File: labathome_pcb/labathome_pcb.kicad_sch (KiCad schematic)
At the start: 48 parts, among them J11 USB_ESP32, J15 CAN RS 485, J17 Micro_SD_Card_Det1, J21 GPIO, J22 Volts, J6 I2C, J7 PROG ESP, Q6 IRLML6344, SW2 YELLOW, SW3 GREEN, SW3 Reset, SW4 RED, U2 ESP32-S3-WROOM-1, U3 SRV05-4, X2 Display_1.3inch

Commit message: Optimized PCB
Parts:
- removed JP6, JP7: STEP3_EN, Jumper:SolderJumper-2_P1.3mm_Bridged2Bar_RoundedPad1.0x1.5mm, symbol Jumper:Jumper_2_Bridged
- added J18: TC-2030, Connector:Tag-Connect_TC2030-IDC-NL_2x03_P1.27mm_Vertical, symbol Connector:Conn_ARM_SWD_TagConnect_TC2030-NL
- J7: footprint liebler_CONN:PinHeader_2x03_P1.27mm_Vertical_SMD_handsolder -> Connector:Tag-Connect_TC2030-IDC-NL_2x03_P1.27mm_Vertical
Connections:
- net +3V3: now also J18.1 (VCC)
- net GND: now also J18.5 (GND)
- net at U2.28 (SPIIO6/GPIO35/FSPID/SUBSPID): now also JP3.1 (A)
- net at U2.30 (SPIDQS/GPIO37/FSPIQ/SUBSPIQ): no longer JP3.1 (A)
- new net STM32_RESET: J18.3 (~{RESET})
- new net SWCLK: J18.4 (SWCLK)
- new net SWDIO: J18.2 (SWDIO)
- new net UART4_TX: J18.6 (SWO)
- no-connect marks 5 -> 7

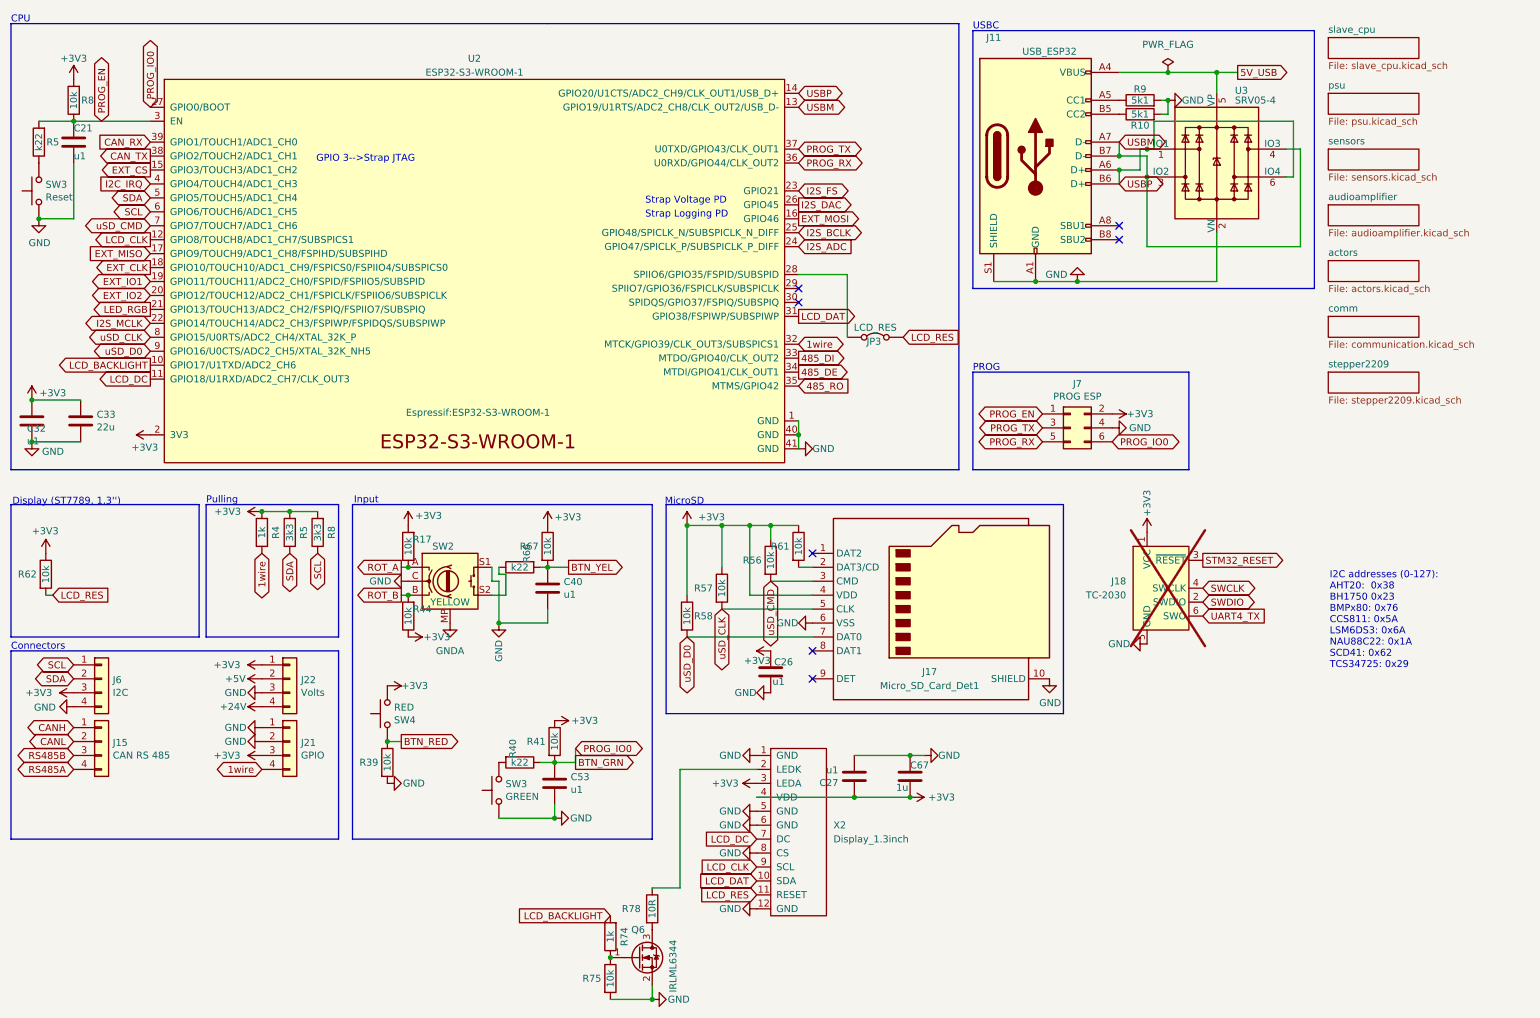
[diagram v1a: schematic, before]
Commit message: Continued with severe refactoring. Now builds, but completely untested
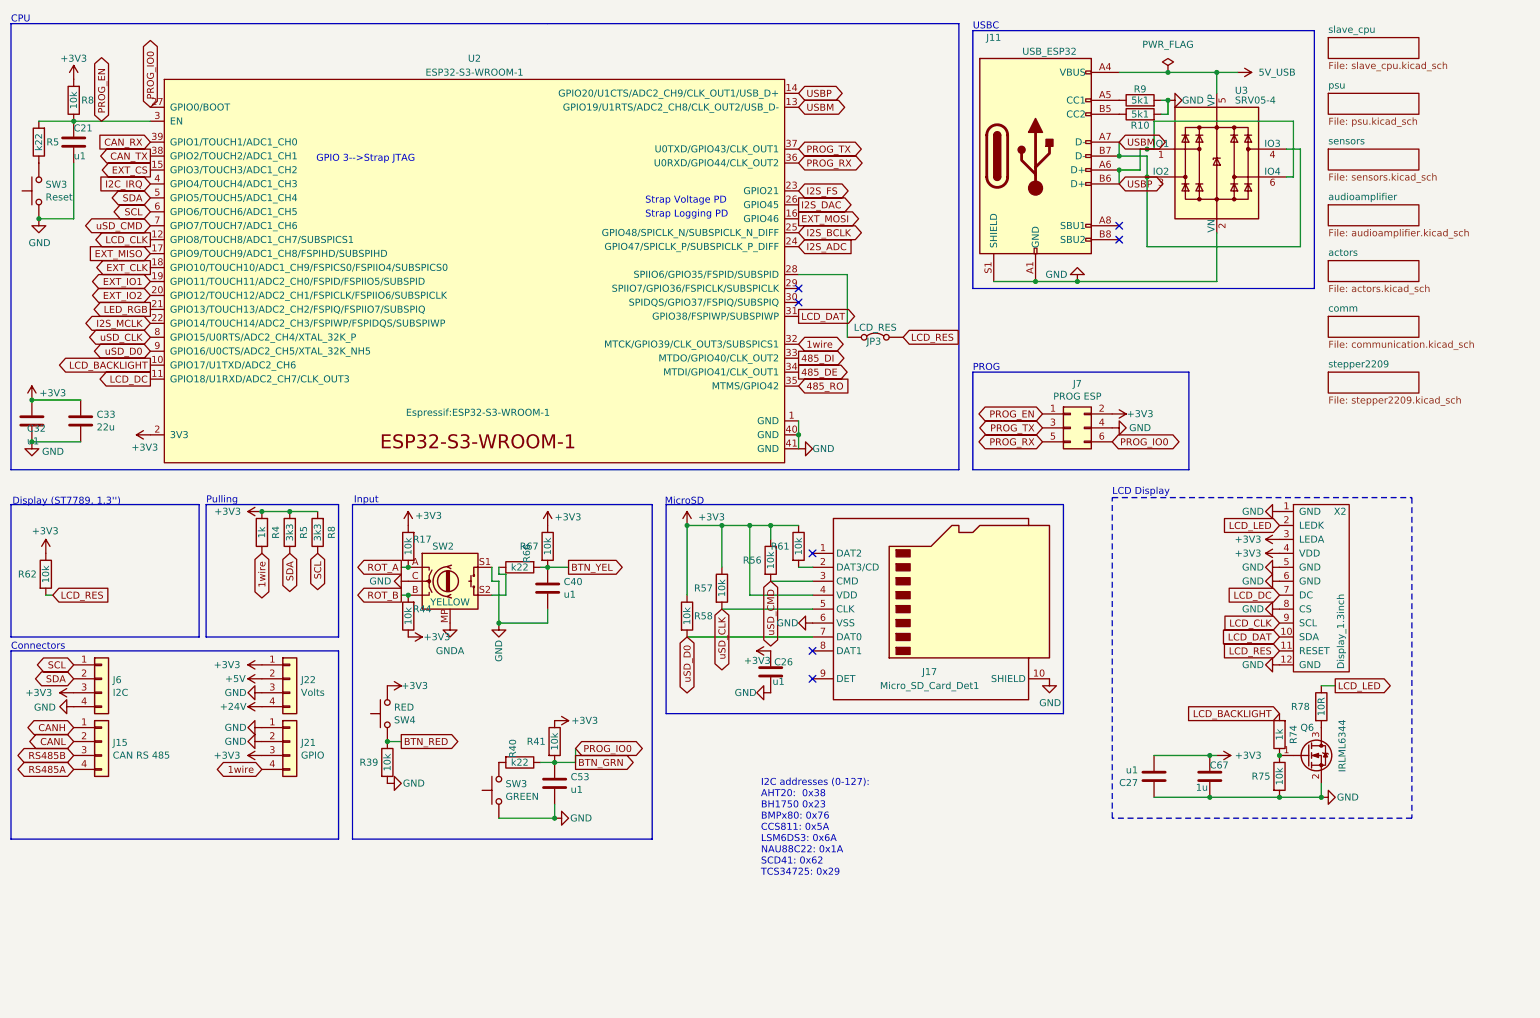
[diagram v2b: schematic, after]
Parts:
- removed J18: TC-2030, Connector:Tag-Connect_TC2030-IDC-NL_2x03_P1.27mm_Vertical, symbol Connector:Conn_ARM_SWD_TagConnect_TC2030-NL
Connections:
- net +3V3: now also C27.2, C67.1; no longer C27.1, C67.2
- net GND: now also C27.1, C67.2; no longer C27.2, C67.1
- net LCD_LED: now reaches R78.1, X2.2 (LEDK)
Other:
- note added: "LCD Display"
- moved on the sheet: C27, C67, Q6, R74, R75, R78, X2

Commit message: Bus servos
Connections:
- net +24V renamed 5-24V
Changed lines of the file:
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@@
-	)
-	(symbol
-		(lib_id "power:+24V")
-		(at 58.42 138.43 90)
-		(unit 1)
-		(exclude_from_sim no)
-		(in_bom yes)
-		(on_board yes)
-		(dnp no)
-		(property "Reference" "#PWR0111"
-			(at 62.23 138.43 0)
-			(effects
-				(font
-					(size 1.27 1.27)
-				)
-				(hide yes)
-			)
-		)
-		(property "Value" "+24V"
-			(at 55.626 138.43 90)
-			(effects
-				(font
-					(size 1.27 1.27)
-				)
-				(justify left)
-			)
-		)
-		(property "Footprint" ""
-			(at 58.42 138.43 0)
-			(effects
-				(font
-					(size 1.27 1.27)
-				)
-				(hide yes)
-			)
-		)
-		(property "Datasheet" ""
-			(at 58.42 138.43 0)
-			(effects
-				(font
-					(size 1.27 1.27)
-				)
-				(hide yes)
-			)
-		)
-		(property "Description" "Power symbol creates a global label with name \"+24V\""
-			(at 58.42 138.43 0)
-			(effects
-				(font
-					(size 1.27 1.27)
-				)
-				(hide yes)
-			)
-		)
-		(pin "1"
-		)
-		(instances
-			(project "labathome_pcb15"
-				(path "/e4d6926a-1a8b-424d-97c4-66b6ad87e4ac"
-					(reference "#PWR0111")
-					(unit 1)
-				)
-			)
-		)
 	)
 	(symbol
@@
 					(unit 1)
 				)
+			)
+		)
+	)
+	(symbol
+		(lib_id "power:+VSW")
+		(at 58.42 138.43 90)
+		(unit 1)
+		(exclude_from_sim no)
+		(in_bom yes)
+		(on_board yes)
+		(dnp no)
+		(fields_autoplaced yes)
+		(property "Reference" "#PWR076"
+			(at 62.23 138.43 0)
+			(effects
+				(font
+					(size 1.27 1.27)
+				)
+				(hide yes)
+			)
+		)
+		(property "Value" "5-24V"
+			(at 54.61 138.4299 90)
+			(effects
+				(font
+					(size 1.27 1.27)
+				)
+				(justify left)
+			)
+		)
+		(property "Footprint" ""
+			(at 58.42 138.43 0)
+			(effects
+				(font
+					(size 1.27 1.27)
+				)
+				(hide yes)
+			)
+		)
+		(property "Datasheet" ""
+			(at 58.42 138.43 0)
+			(effects
+				(font
+					(size 1.27 1.27)
+				)
+				(hide yes)
+			)
+		)
+		(property "Description" "Power symbol creates a global label with name \"+VSW\""
+			(at 58.42 138.43 0)
+			(effects
+				(font
+					(size 1.27 1.27)
+				)
+				(hide yes)
+			)
+		)
+		(pin "1"
+		)
+		(instances
+			(project "labathome_pcb"
+				(path "/e4d6926a-1a8b-424d-97c4-66b6ad87e4ac"
+					(reference "#PWR076")
+					(unit 1)
+				)

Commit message: Minor improments on pcb
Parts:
- J11: footprint liebler_CONN:USB_C_Receptacle_HRO_TYPE-C-31-M-12_IMPROVED -> liebler_CONN:USB_C_Receptacle_HRO_TYPE-C-31-M-12_smaller
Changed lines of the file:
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@@
 			)
 		)
-		(property "Footprint" "liebler_CONN:USB_C_Receptacle_HRO_TYPE-C-31-M-12_IMPROVED"
+		(property "Footprint" "liebler_CONN:USB_C_Receptacle_HRO_TYPE-C-31-M-12_smaller"
 			(at 203.2 38.1 0)
 			(effects

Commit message: Minor changes
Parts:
- C21, C26, C27, C32, C40, C53: MPN (none) -> GRM033R61A104KE15D; Manufacturer (none) -> Murata Electronics
- C33: MPN (none) -> CL10A226MP8NUNE; Manufacturer (none) -> Samsung Electro-Mechanics
- C67: MPN (none) -> CL05A105KA5NQNC; Manufacturer (none) -> Samsung Electro-Mechanics
- J11: MPN (none) -> TYPE-C-31-M-12; Manufacturer (none) -> Korean Hroparts Elec
- J15, J21, J22, J6: MPN (none) -> KF2EDGR-3.5-4P; Manufacturer (none) -> Cixi Kefa Elec
- J17: MPN (none) -> TF PUSH; Manufacturer (none) -> SHOU HAN
- Q6: MPN (none) -> AO3400; Manufacturer (none) -> GOODWORK
- R10, R9: MPN (none) -> RC0201FR-075K1L; Manufacturer (none) -> YAGEO
- R17, R39, R41, R44, R56, R57, R58, R61, R62, R67, R75, R8: MPN (none) -> 0201WMF1002TEE; Manufacturer (none) -> UNI-ROYAL(Uniroyal Elec)
- R4, R74: MPN (none) -> 0402WGF1001TCE; Manufacturer (none) -> UNI-ROYAL(Uniroyal Elec)
- R40, R5, R66: MPN (none) -> 0402WGF2200TCE; Manufacturer (none) -> UNI-ROYAL(Uniroyal Elec)
- R5, R8: MPN (none) -> 0402WGF3301TCE; Manufacturer (none) -> UNI-ROYAL(Uniroyal Elec)
- R78: MPN (none) -> 1206W4F100JT5E; Manufacturer (none) -> UNI-ROYAL(Uniroyal Elec)
- SW2: MPN (none) -> EC11E0940501; Manufacturer (none) -> ALPSALPINE
- SW3: MPN (none) -> TS24CA 250gf 013; Manufacturer (none) -> SHOU HAN
- SW3, SW4: MPN (none) -> TS-1095E-A6B3-D2; Manufacturer (none) -> Yuandi
- U2: MPN (none) -> ESP32-S3-WROOM-1-N8R2; Manufacturer (none) -> Espressif Systems
- U3: MPN (none) -> SRV05-4; Manufacturer (none) -> MSKSEMI

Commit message: Labathome PCB -> KICAD 9
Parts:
- renumbered C32 to C2, C21 to C5, C33 to C6, J6 to J2, J11 to J5, J7 to J6, R5 to R1, R9 to R18, R10 to R19, R8 to R2, R17 to R36, R44 to R37, R4 to R42, R5 to R43, R8 to R44, SW3 to SW1, SW2 to SW6, SW4 to SW7, SW3 to SW8, U2 to U4, U3 to U8
